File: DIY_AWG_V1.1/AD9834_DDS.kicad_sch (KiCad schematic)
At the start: 66 parts, among them IC1 ADG704BRMZ-REEL7, IC2 TLV3544IPWR, U11 8121H-50.000NK33DRL, U12 AD9834, U16 OPA2171AIDR

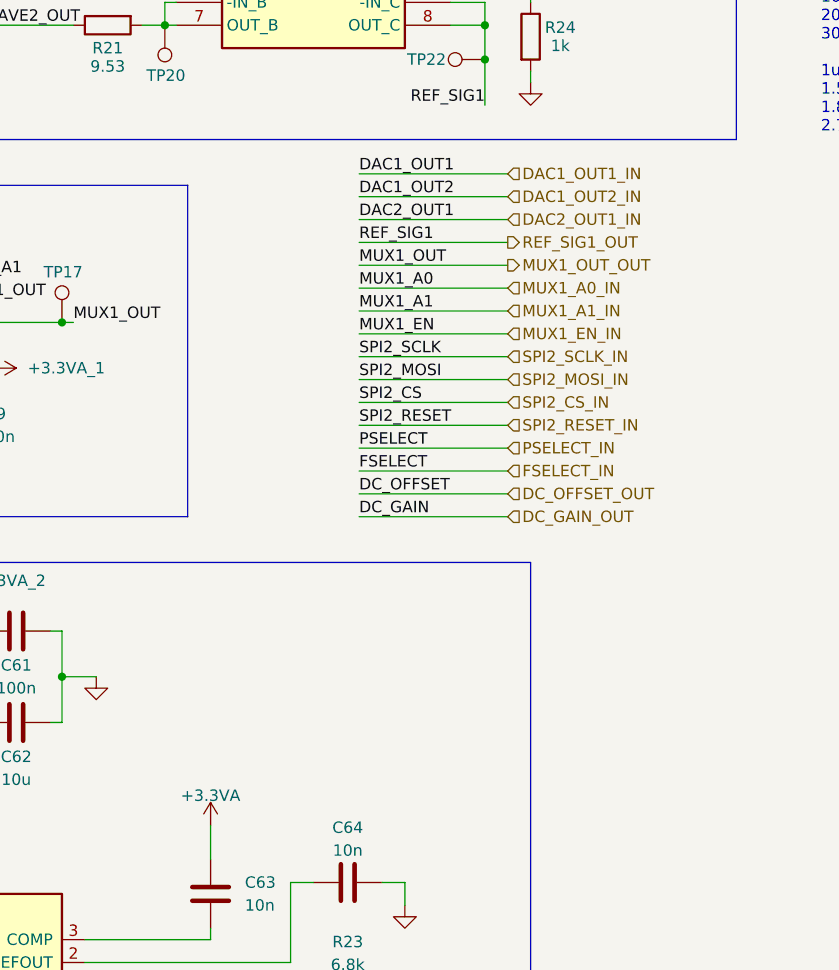
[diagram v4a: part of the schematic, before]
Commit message: Updated schematics to clear ERCs
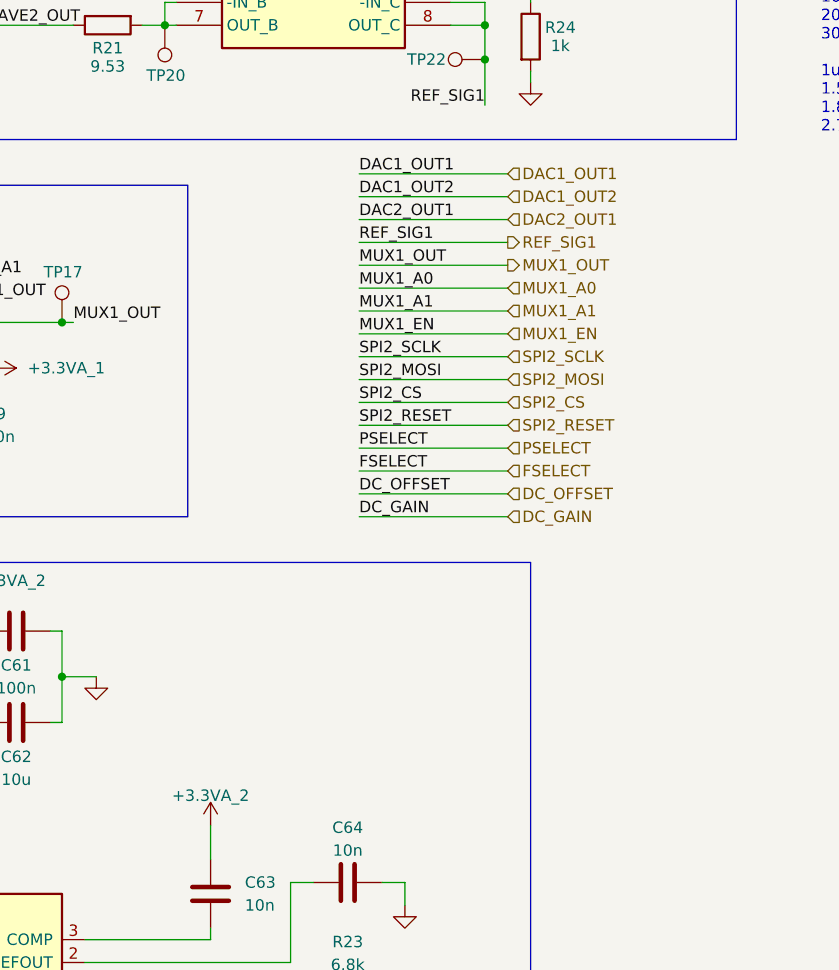
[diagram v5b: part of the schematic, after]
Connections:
- net +3.3VA is gone; now on net +3.3VA_2: C63.2
- net DAC1_OUT1_IN renamed DAC1_OUT1
- net DAC1_OUT2_IN renamed DAC1_OUT2
- net DAC2_OUT1_IN renamed DAC2_OUT1
- net DC_GAIN_OUT renamed DC_GAIN
- net DC_OFFSET_OUT renamed DC_OFFSET
- net FSELECT_IN renamed FSELECT
- net MUX1_A0_IN renamed MUX1_A0
- net MUX1_A1_IN renamed MUX1_A1
- net MUX1_EN_IN renamed MUX1_EN
- net MUX1_OUT_OUT renamed MUX1_OUT
- net PSELECT_IN renamed PSELECT
- net REF_SIG1_OUT renamed REF_SIG1
- net SPI2_CS_IN renamed SPI2_CS
- net SPI2_MOSI_IN renamed SPI2_MOSI
- net SPI2_RESET_IN renamed SPI2_RESET
- net SPI2_SCLK_IN renamed SPI2_SCLK
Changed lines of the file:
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@@
 		)
 	)
-	(hierarchical_label "SPI2_SCLK_IN"
+	(hierarchical_label "SPI2_SCLK"
 		(shape input)
 		(at 149.86 118.11 0)
@@
 		)
 	)
-	(hierarchical_label "MUX1_A0_IN"
+	(hierarchical_label "MUX1_A0"
 		(shape input)
 		(at 149.86 110.49 0)
@@
 		)
 	)
-	(hierarchical_label "REF_SIG1_OUT"
+	(hierarchical_label "REF_SIG1"
 		(shape output)
 		(at 149.86 105.41 0)
@@
 		)
 	)
-	(hierarchical_label "SPI2_RESET_IN"
+	(hierarchical_label "SPI2_RESET"
 		(shape input)
 		(at 149.86 125.73 0)
@@
 		)
 	)
-	(hierarchical_label "DC_GAIN_OUT"
+	(hierarchical_label "DC_GAIN"
 		(shape input)
 		(at 149.86 135.89 0)
@@
 		)
 	)
-	(hierarchical_label "PSELECT_IN"
+	(hierarchical_label "PSELECT"
 		(shape input)
 		(at 149.86 128.27 0)
@@
 		)
 	)
-	(hierarchical_label "FSELECT_IN"
+	(hierarchical_label "FSELECT"
 		(shape input)
 		(at 149.86 130.81 0)
@@
 		)
 	)
-	(hierarchical_label "MUX1_EN_IN"
+	(hierarchical_label "MUX1_EN"
 		(shape input)
 		(at 149.86 115.57 0)
@@
 		)
 	)
-	(hierarchical_label "DAC2_OUT1_IN"
+	(hierarchical_label "DAC2_OUT1"
 		(shape input)
 		(at 149.86 102.87 0)
@@
 		)
 	)
-	(hierarchical_label "DAC1_OUT1_IN"
+	(hierarchical_label "DAC1_OUT1"
 		(shape input)
 		(at 149.86 97.79 0)
@@
 		)
 	)
-	(hierarchical_label "DC_OFFSET_OUT"
+	(hierarchical_label "DC_OFFSET"
 		(shape input)
 		(at 149.86 133.35 0)
@@
 		)
 	)
-	(hierarchical_label "SPI2_CS_IN"
+	(hierarchical_label "SPI2_CS"
 		(shape input)
 		(at 149.86 123.19 0)
@@
 		)
 	)
-	(hierarchical_label "MUX1_OUT_OUT"
+	(hierarchical_label "MUX1_OUT"
 		(shape output)
 		(at 149.86 107.95 0)
@@
 		)
 	)
-	(hierarchical_label "DAC1_OUT2_IN"
+	(hierarchical_label "DAC1_OUT2"
 		(shape input)
 		(at 149.86 100.33 0)
@@
 		)
 	)
-	(hierarchical_label "MUX1_A1_IN"
+	(hierarchical_label "MUX1_A1"
 		(shape input)
 		(at 149.86 113.03 0)
@@
 		)
 	)
-	(hierarchical_label "SPI2_MOSI_IN"
+	(hierarchical_label "SPI2_MOSI"
 		(shape input)
 		(at 149.86 120.65 0)
@@
 			)
 		)
-		(property "Value" "+3.3VA"
+		(property "Value" "+3.3VA_2"
 			(at 116.84 166.878 0)
 			(show_name no)

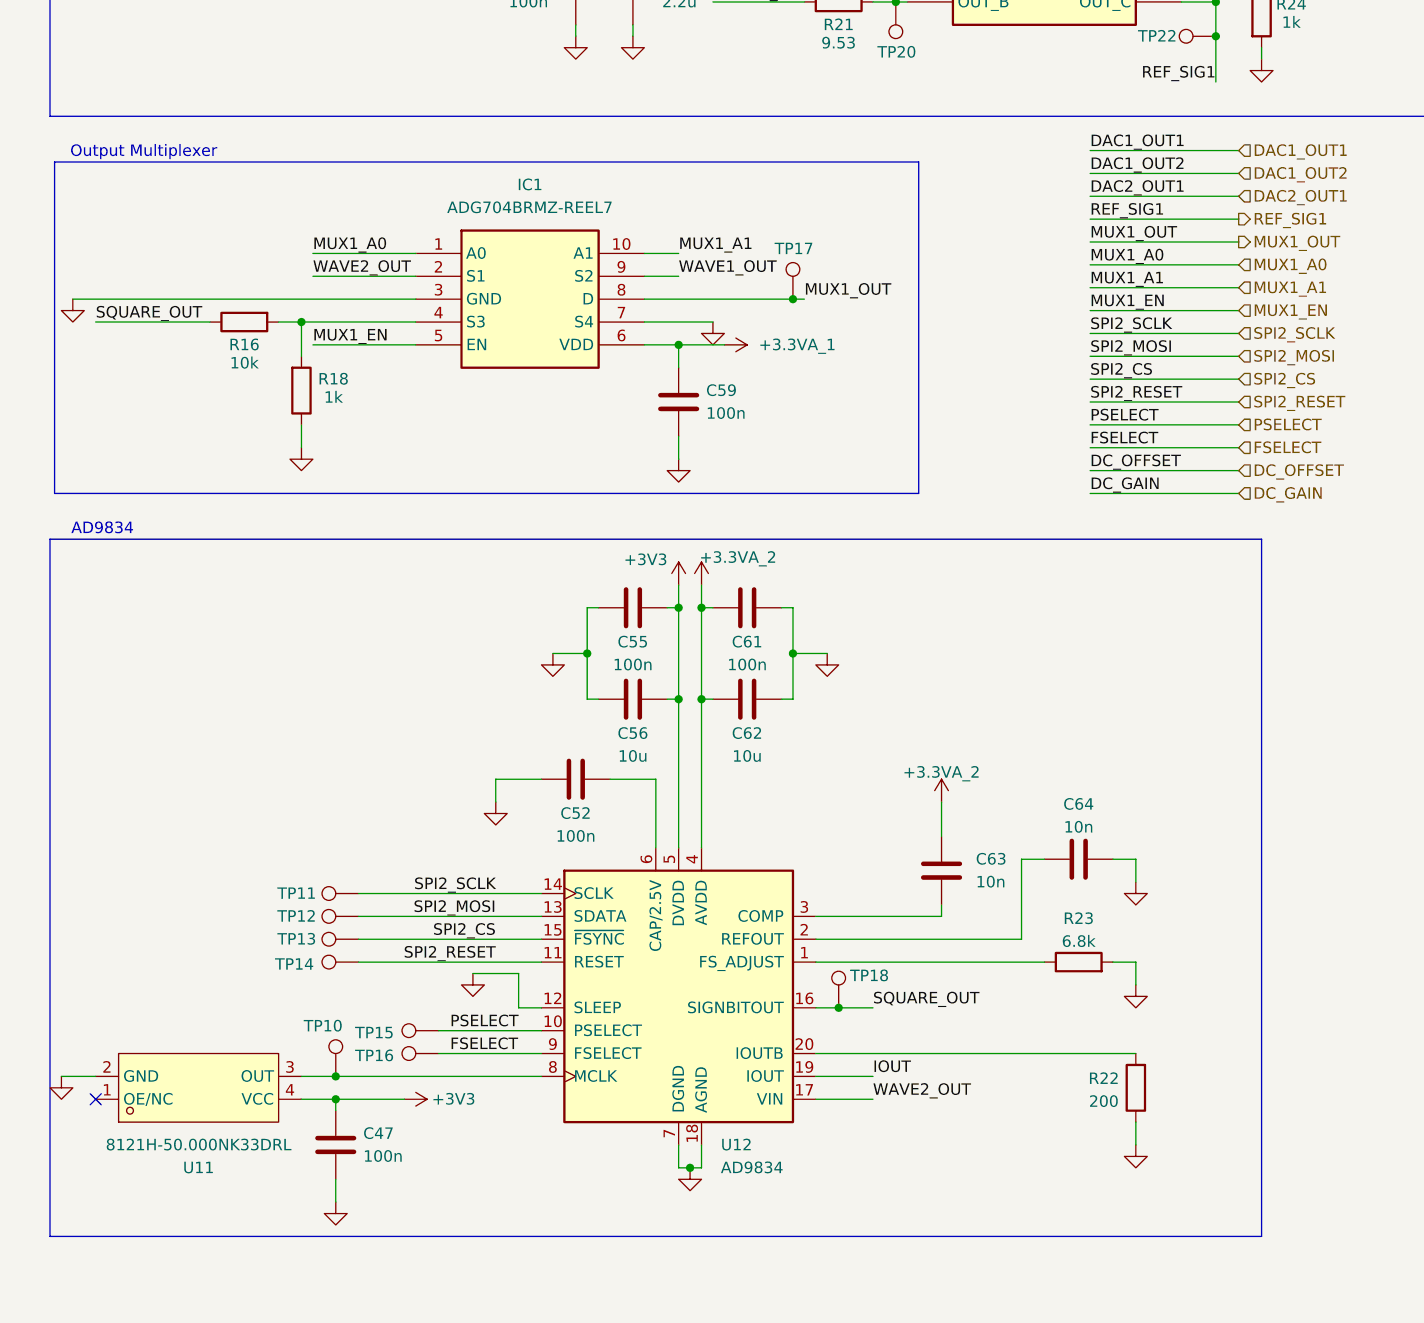
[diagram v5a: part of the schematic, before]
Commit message: Updated the schematics to resolve ERCs
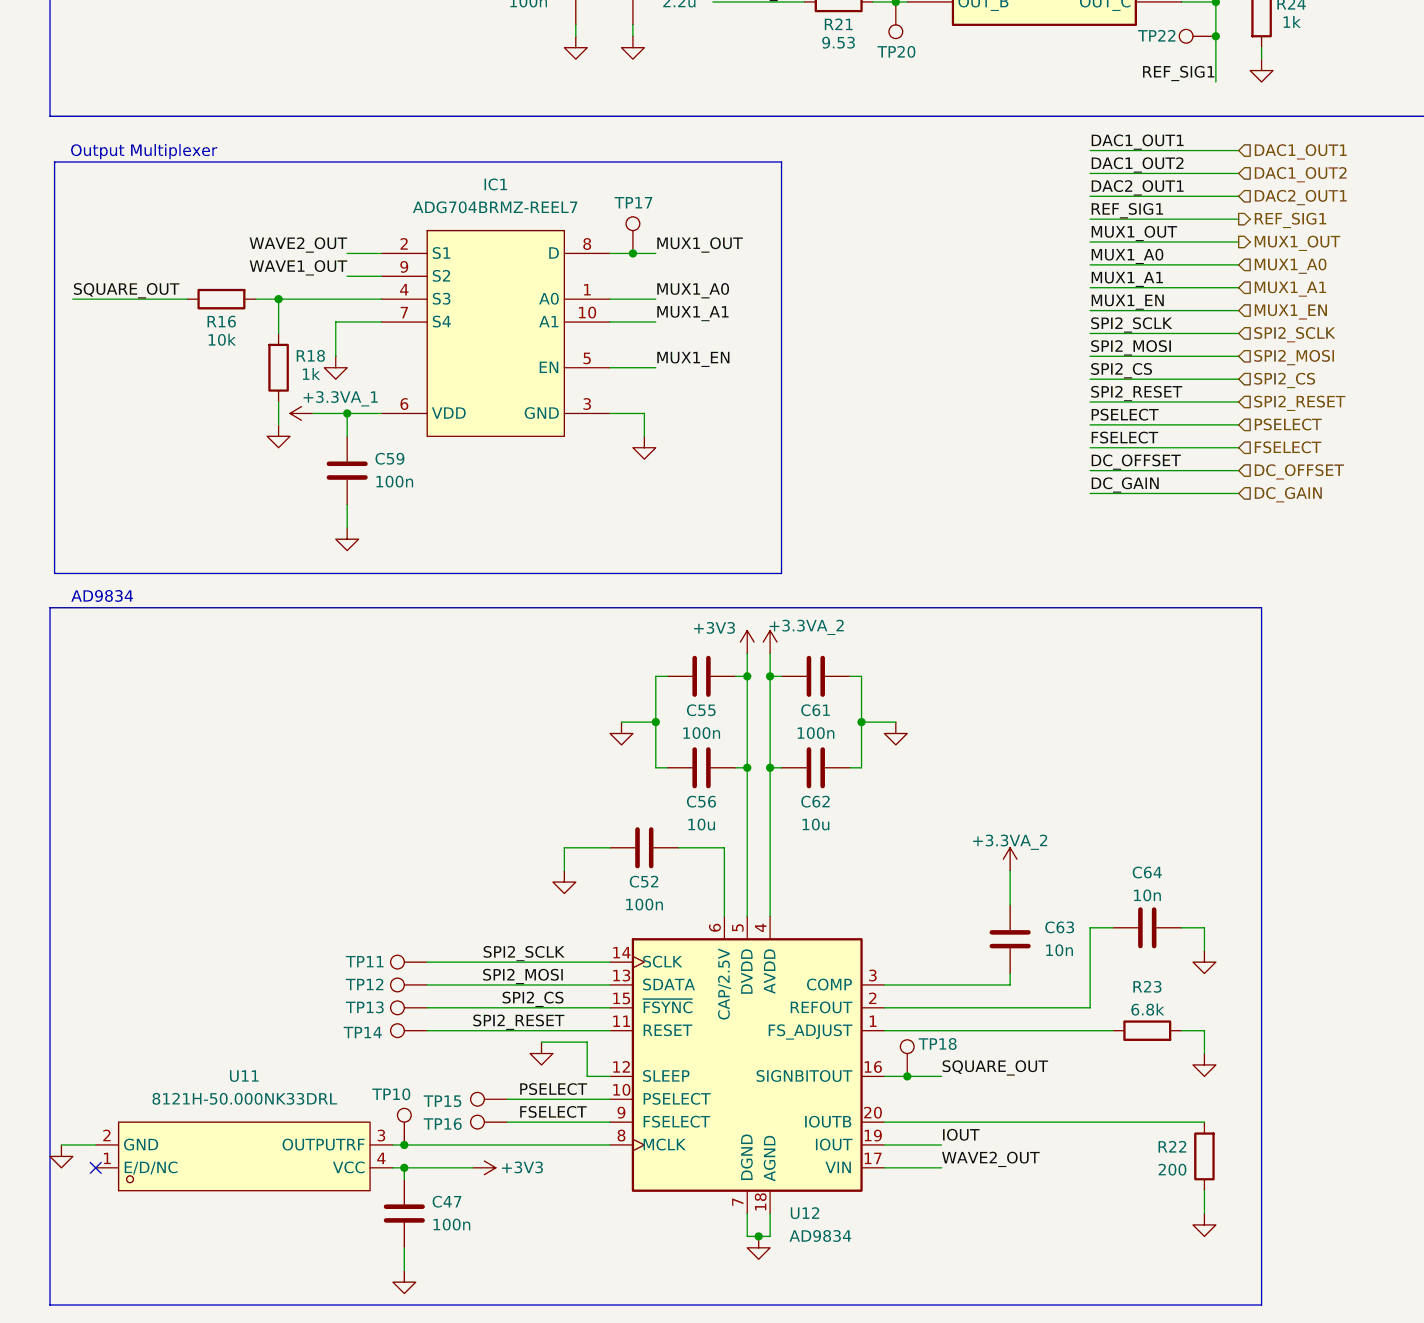
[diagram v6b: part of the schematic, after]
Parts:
- removed IC1: ADG704BRMZ-REEL7, SOP50P490X110-10N, symbol ADG704BRMZ-REEL7:ADG704BRMZ-REEL7
- removed U11: 8121H-50.000NK33DRL, easyeda2kicad:OSC-SMD_4P-L2.0-W1.6-BL_SIT8008BI-72-33E-54.000000, symbol easyeda2kicad:8121H-50.000NK33DRL
- added IC1: ADG704BRMZ-REEL7, easyeda2kicad:MSOP-10_L3.0-W3.0-P0.50-LS5.0-BL, symbol easyeda2kicad:ADG704BRMZ
- added U11: 8121H-50.000NK33DRL, easyeda2kicad:OSC-SMD_4P-L3.2-W2.5-BL, symbol easyeda2kicad:8132H-50.000ML33DTL
- IC2: footprint SOP65P640X120-14N -> easyeda2kicad:TSSOP-14_L5.0-W4.4-P0.65-LS6.4-BL
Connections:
- net +3.3VA_1: now also IC1.6 (VDD)
- net +3V3: now also U11.4 (VCC)
- net GND: now also IC1.3 (GND), IC1.7 (S4), U11.2 (GND)
- net MUX1_A0: now also IC1.1 (A0)
- net MUX1_A1: now also IC1.10 (A1)
- net MUX1_EN: now also IC1.5 (EN)
- net MUX1_OUT: now also IC1.8 (D)
- net WAVE1_OUT: now also IC1.9 (S2)
- net WAVE2_OUT: now also IC1.2 (S1)
- net at TP10.1, U12.8 (MCLK): now also U11.3 (OUTPUTRF)
- net at R16.2, R18.2: now also IC1.4 (S3)
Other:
- moved on the sheet: C47, C52, C55, C56, C61, C62, C63, C64, R22, R23, TP10, TP11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

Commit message: Updated to fix all ERCs
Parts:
- removed IC2: TLV3544IPWR, easyeda2kicad:TSSOP-14_L5.0-W4.4-P0.65-LS6.4-BL, symbol TLV3544IPWR:TLV3544IPWR
- removed U11: 8121H-50.000NK33DRL, easyeda2kicad:OSC-SMD_4P-L3.2-W2.5-BL, symbol easyeda2kicad:8132H-50.000ML33DTL
- added IC2: TLV3544IPWR, easyeda2kicad:TSSOP-14_L5.0-W4.4-P0.65-LS6.4-BL, symbol easyeda2kicad:TLV3544IPWR
- added U11: 8121H-50.000NK33DRL, easyeda2kicad:OSC-SMD_4P-L2.0-W1.6-BL_SIT8008BI-72-33E-54.000000, symbol easyeda2kicad:8121H-50.000NK33DRL
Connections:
- net +3.3VA_1: now also IC2.4 (V+)
- net +3V3: now also U11.4 (VCC)
- net DAC1_OUT1: now also IC2.3 (INA+)
- net GND: now also IC2.11 (V-), IC2.12 (IND+), U11.2 (GND)
- net REF_SIG1: now also IC2.8 (OUTC), IC2.9 (INC-)
- net VOUT: now also IC2.5 (INB+)
- net WAVE2_OUT: now also R21.2; no longer R21.1
- net at TP10.1, U12.8 (MCLK): now also U11.3 (OUT)
- net at C49.2, L7.2: now also R20.2; no longer R20.1
- net at TP19.1: now also R20.1, IC2.1 (OUTA), IC2.2 (INA-); no longer R20.2
- net at TP20.1: now also R21.1, IC2.6 (INB-), IC2.7 (OUTB); no longer R21.2
- net at R24.1, R25.1: now also IC2.10 (INC+)
- new net: IC2.13 (IND-), IC2.14 (OUTD)
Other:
- moved on the sheet: C47, C52, C55, C56, C59, C61, C62, C63, C64, IC1, R16, R18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

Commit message: Updated component footprints
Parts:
- added TP22: TestPoint, symbol Connector:TestPoint
- renumbered C59 to C46, C57 to C47, C47 to C49, C53 to C50, C50 to C51, C51 to C52, C49 to C53, C46 to C55, C52 to C56, C58 to C57, C55 to C58, C56 to C59, C74 to C65, C79 to C66, C75 to C67, C76 to C68, C77 to C69, C78 to C70, IC2 to IC1, IC1 to IC2, L8 to L7, L9 to L8, L7 to L9, R16 to R15, R18 to R16, R20 to R17, R21 to R18, R17 to R19, R15 to R20, R19 to R21, R25 to R22, R24 to R23, R23 to R24, R22 to R25, R31 to R26, R32 to R27, R41 to R28, R30 to R29, TP10 to TP12, TP11 to TP13, TP12 to TP14, TP13 to TP15, TP14 to TP16, TP19 to TP17, TP20 to TP18, TP15 to TP19, TP16 to TP20, TP17 to TP21, TP18 to TP23, TP22 to TP24, TP24 to TP26, U16 to U13
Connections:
- net WAVE1_OUT: now also TP22.1
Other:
- moved on the sheet: C46, C49, C56, C58, C59, C61, C62, C63, C64, IC2, R15, R16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
